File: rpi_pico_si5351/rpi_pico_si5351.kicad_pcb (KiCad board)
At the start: 4 copper layers, 100 x 50 mm, 39 parts, among them J1 CLK0, J2 CLK1, J3 CLK2, J4 SSM-120-F-DV, SW1 JS5208, SW2 PEC12R-3220F-S0024, U1 ER-TFT020-2, U2 RP2040-PICO30, U3 MS5351M, X1 MCSJK-7U-27.00-10-10-60-B-10

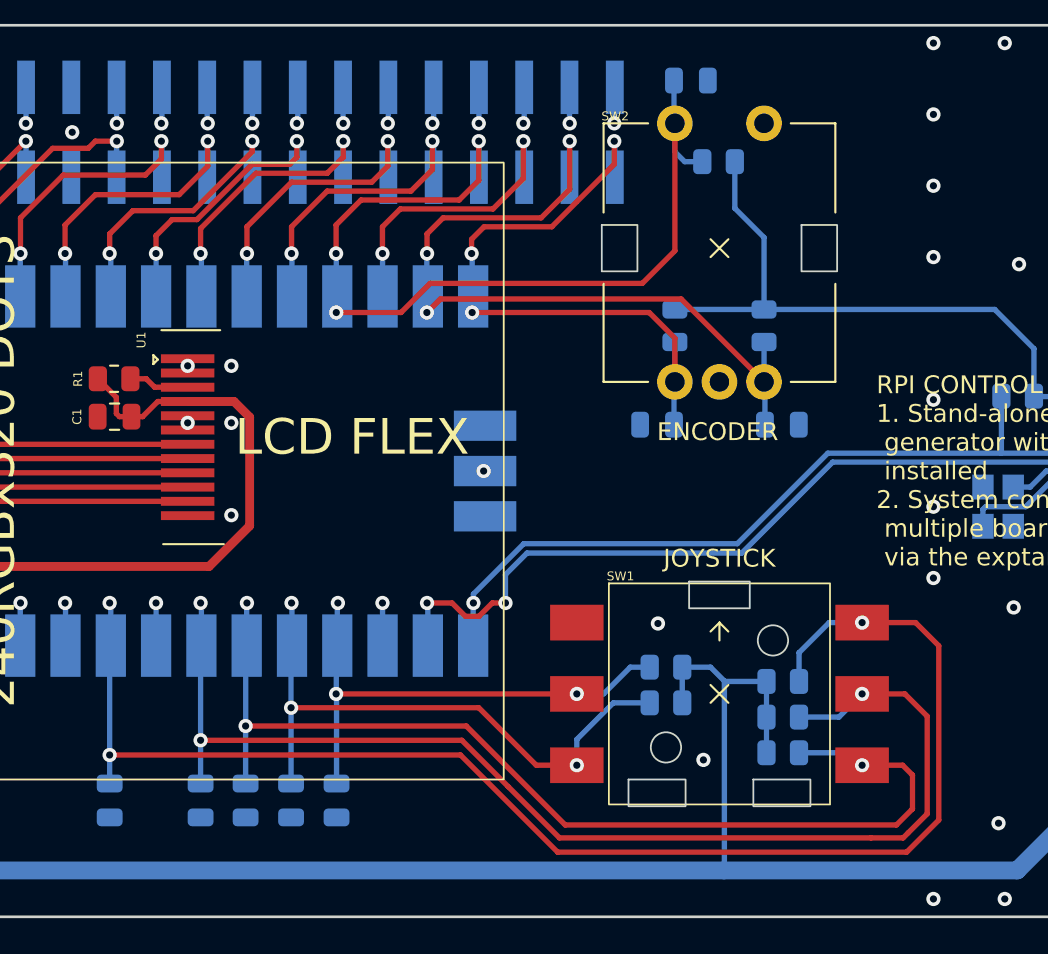
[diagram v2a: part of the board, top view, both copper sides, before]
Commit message: clean-up, add STACk connector
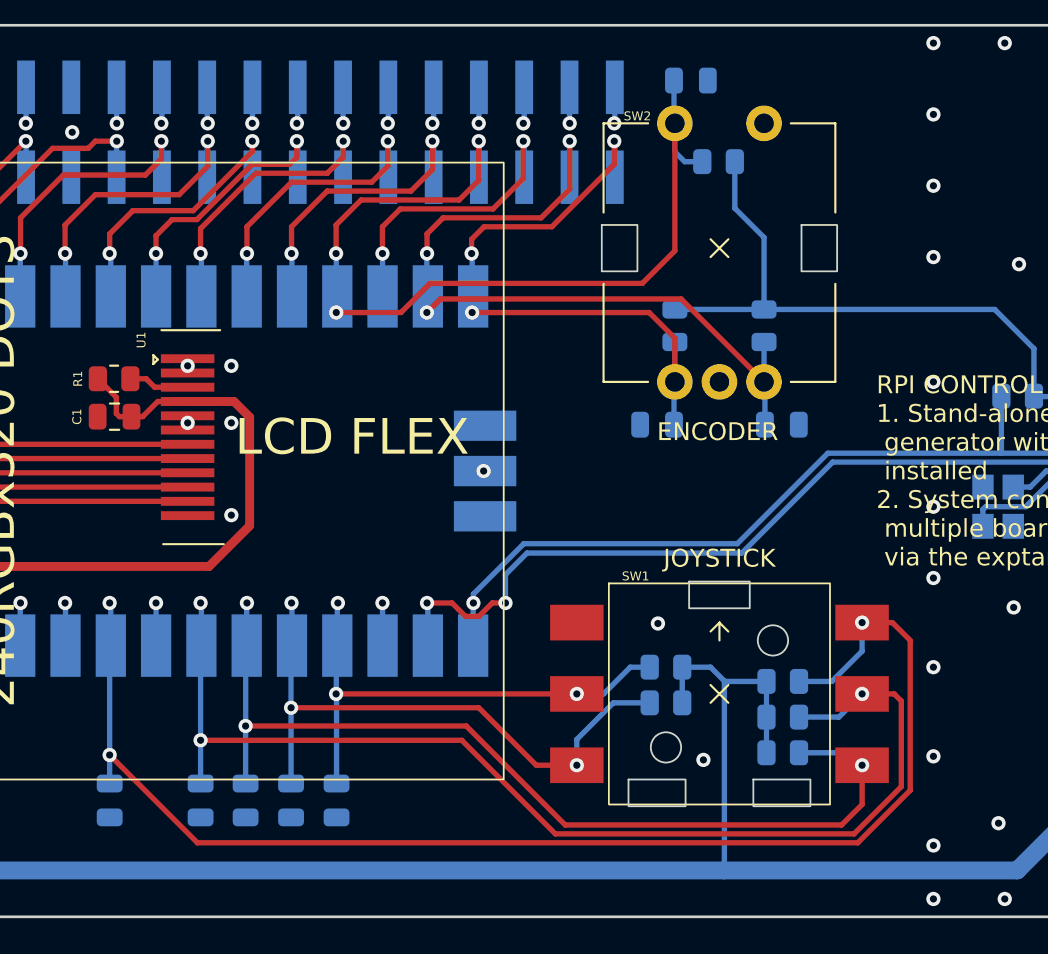
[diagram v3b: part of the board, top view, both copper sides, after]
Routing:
- net GPIO20: track 91.8 -> 86.3 mm
- net GPIO22: track 113.1 -> 108.7 mm
- net GPIO21: track 100.4 -> 96.9 mm
- net GND: vias 48 -> 51
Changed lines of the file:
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@@
     (property "Sheetname" "")
     (attr through_hole)
-    (fp_text reference "SW2" (at -5.85 -7.4 unlocked) (layer "F.SilkS")
+    (fp_text reference "SW2" (at -4.6 -7.4 unlocked) (layer "F.SilkS")
       (effects (font (size 0.5 0.5) (thickness 0.1)))
     )
@@
     (property "Sheetname" "")
     (attr smd)
-    (fp_text reference "SW1" (at -5.55 -6.6 unlocked) (layer "F.SilkS")
+    (fp_text reference "SW1" (at -4.7 -6.6 unlocked) (layer "F.SilkS")
       (effects (font (size 0.5 0.5) (thickness 0.1)))
     )
@@
   (via (at 124.95 52.5) (size 0.8) (drill 0.4) (layers "F.Cu" "B.Cu") (free) (net 1))
   (via (at 106 38) (size 0.8) (drill 0.4) (layers "F.Cu" "B.Cu") (free) (net 1))
+  (via (at 106 71) (size 0.8) (drill 0.4) (layers "F.Cu" "B.Cu") (free) (net 1))
   (via (at 37 37.8) (size 0.8) (drill 0.4) (layers "F.Cu" "B.Cu") (net 1))
   (via (at 106 34) (size 0.8) (drill 0.4) (layers "F.Cu" "B.Cu") (free) (net 1))
@@
   (via (at 116.15 64.35) (size 0.8) (drill 0.4) (layers "F.Cu" "B.Cu") (free) (net 1))
   (via (at 116.15 55.1) (size 0.8) (drill 0.4) (layers "F.Cu" "B.Cu") (free) (net 1))
+  (via (at 106 61) (size 0.8) (drill 0.4) (layers "F.Cu" "B.Cu") (free) (net 1))
   (via (at 118 26) (size 0.8) (drill 0.4) (layers "F.Cu" "B.Cu") (free) (net 1))
   (via (at 110 74) (size 0.8) (drill 0.4) (layers "F.Cu" "B.Cu") (free) (net 1))
@@
   (via (at 122.4 46.9) (size 0.8) (drill 0.4) (layers "F.Cu" "B.Cu") (free) (net 1))
   (via (at 80.775 50) (size 0.8) (drill 0.4) (layers "F.Cu" "B.Cu") (net 1))
+  (via (at 106 66) (size 0.8) (drill 0.4) (layers "F.Cu" "B.Cu") (free) (net 1))
   (via (at 106 74) (size 0.8) (drill 0.4) (layers "F.Cu" "B.Cu") (free) (net 1))
   (via (at 122 74) (size 0.8) (drill 0.4) (layers "F.Cu" "B.Cu") (free) (net 1))
   (via (at 110.5 57.65) (size 0.8) (drill 0.4) (layers "F.Cu" "B.Cu") (free) (net 1))
   (via (at 114 26) (size 0.8) (drill 0.4) (layers "F.Cu" "B.Cu") (free) (net 1))
-  (via (at 106 46) (size 0.8) (drill 0.4) (layers "F.Cu" "B.Cu") (free) (net 1))
+  (via (at 106 45) (size 0.8) (drill 0.4) (layers "F.Cu" "B.Cu") (free) (net 1))
   (via (at 124.95 59.5) (size 0.8) (drill 0.4) (layers "F.Cu" "B.Cu") (free) (net 1))
   (via (at 118 74) (size 0.8) (drill 0.4) (layers "F.Cu" "B.Cu") (free) (net 1))
@@
   (segment (start 72.565 58.89) (end 72.565 57.435) (width 0.3) (layer "B.Cu") (net 39))
   (segment (start 89 61) (end 90.0875 61) (width 0.3) (layer "B.Cu") (net 39))
-  (segment (start 105 58.5) (end 106.3 59.8) (width 0.3) (layer "F.Cu") (net 40))
-  (segment (start 106.3 69.575) (end 104.5 71.375) (width 0.3) (layer "F.Cu") (net 40))
-  (segment (start 106.3 59.8) (end 106.3 69.575) (width 0.3) (layer "F.Cu") (net 40))
-  (segment (start 79.475 65.925) (end 59.8 65.925) (width 0.3) (layer "F.Cu") (net 40))
-  (segment (start 84.925 71.375) (end 79.475 65.925) (width 0.3) (layer "F.Cu") (net 40))
-  (segment (start 104.5 71.375) (end 84.925 71.375) (width 0.3) (layer "F.Cu") (net 40))
-  (segment (start 102 58.5) (end 105 58.5) (width 0.3) (layer "F.Cu") (net 40))
+  (segment (start 104.7 67.907106) (end 101.757106 70.85) (width 0.3) (layer "F.Cu") (net 40))
+  (segment (start 103.7 58.5) (end 104.7 59.5) (width 0.3) (layer "F.Cu") (net 40))
+  (segment (start 64.725 70.85) (end 59.8 65.925) (width 0.3) (layer "F.Cu") (net 40))
+  (segment (start 104.7 59.5) (end 104.7 67.907106) (width 0.3) (layer "F.Cu") (net 40))
+  (segment (start 102 58.5) (end 103.7 58.5) (width 0.3) (layer "F.Cu") (net 40))
+  (segment (start 101.757106 70.85) (end 64.725 70.85) (width 0.3) (layer "F.Cu") (net 40))
   (via (at 59.8 65.925) (size 0.8) (drill 0.4) (layers "F.Cu" "B.Cu") (net 40))
   (via (at 59.8 57.4) (size 0.8) (drill 0.4) (layers "F.Cu" "B.Cu") (net 40))
@@
   (segment (start 59.8 58.9) (end 59.81 58.89) (width 0.3) (layer "B.Cu") (net 40))
   (segment (start 59.865 57.465) (end 59.8 57.4) (width 0.3) (layer "B.Cu") (net 40))
+  (segment (start 98.4625 61.8) (end 100.3 61.8) (width 0.3) (layer "B.Cu") (net 40))
+  (segment (start 100.3 61.8) (end 102 60.1) (width 0.3) (layer "B.Cu") (net 40))
   (segment (start 59.865 58.89) (end 59.865 57.465) (width 0.3) (layer "B.Cu") (net 40))
+  (segment (start 102 60.1) (end 102 58.5) (width 0.3) (layer "B.Cu") (net 40))
   (segment (start 67.81 30.490497) (end 67.8 30.500497) (width 0.3) (layer "B.Cu") (net 40))
   (segment (start 59.8 67.525) (end 59.8 65.925) (width 0.3) (layer "B.Cu") (net 40))
-  (segment (start 98.4625 61.8) (end 98.4625 60.1875) (width 0.3) (layer "B.Cu") (net 40))
   (segment (start 59.8 65.925) (end 59.8 58.9) (width 0.3) (layer "B.Cu") (net 40))
   (segment (start 67.81 28.48) (end 67.81 30.490497) (width 0.3) (layer "B.Cu") (net 40))
-  (segment (start 98.4625 60.1875) (end 100.15 58.5) (width 0.3) (layer "B.Cu") (net 40))
-  (segment (start 100.15 58.5) (end 102 58.5) (width 0.3) (layer "B.Cu") (net 40))
-  (segment (start 104.4 62.5) (end 105.65 63.75) (width 0.3) (layer "F.Cu") (net 41))
-  (segment (start 102 62.5) (end 104.4 62.5) (width 0.3) (layer "F.Cu") (net 41))
-  (segment (start 105.65 63.75) (end 105.65 69.225) (width 0.3) (layer "F.Cu") (net 41))
-  (segment (start 104.575 70.3) (end 104.3 70.575) (width 0.3) (layer "F.Cu") (net 41))
-  (segment (start 82.15 67.7) (end 79.55 65.1) (width 0.3) (layer "F.Cu") (net 41))
+  (segment (start 103.8 62.5) (end 104.2 62.9) (width 0.3) (layer "F.Cu") (net 41))
+  (segment (start 101.55 70.35) (end 84.8 70.35) (width 0.3) (layer "F.Cu") (net 41))
+  (segment (start 104.2 62.9) (end 104.2 67.7) (width 0.3) (layer "F.Cu") (net 41))
+  (segment (start 84.8 70.35) (end 79.55 65.1) (width 0.3) (layer "F.Cu") (net 41))
   (segment (start 79.55 65.1) (end 64.9 65.1) (width 0.3) (layer "F.Cu") (net 41))
-  (segment (start 105.65 69.225) (end 104.575 70.3) (width 0.3) (layer "F.Cu") (net 41))
-  (segment (start 102.5 70.575) (end 85.025 70.575) (width 0.3) (layer "F.Cu") (net 41))
-  (segment (start 104.3 70.575) (end 102.5 70.575) (width 0.3) (layer "F.Cu") (net 41))
-  (segment (start 85.025 70.575) (end 82.15 67.7) (width 0.3) (layer "F.Cu") (net 41))
+  (segment (start 104.2 67.7) (end 101.55 70.35) (width 0.3) (layer "F.Cu") (net 41))
+  (segment (start 102 62.5) (end 103.8 62.5) (width 0.3) (layer "F.Cu") (net 41))
   (via (at 64.9 65.1) (size 0.8) (drill 0.4) (layers "F.Cu" "B.Cu") (net 41))
   (via (at 102 62.5) (size 0.8) (drill 0.4) (layers "F.Cu" "B.Cu") (net 41))
@@
   (segment (start 64.9 65.1) (end 64.9 58.9) (width 0.3) (layer "B.Cu") (net 41))
   (segment (start 64.9 67.525) (end 64.9 65.1) (width 0.3) (layer "B.Cu") (net 41))
+  (segment (start 102 66.5) (end 102 68.7) (width 0.3) (layer "F.Cu") (net 42))
+  (segment (start 102 68.7) (end 100.85 69.85) (width 0.3) (layer "F.Cu") (net 42))
   (segment (start 79.8 64.3) (end 67.425 64.3) (width 0.3) (layer "F.Cu") (net 42))
-  (segment (start 104.825 68.95) (end 103.925 69.85) (width 0.3) (layer "F.Cu") (net 42))
-  (segment (start 104.275 66.5) (end 104.825 67.05) (width 0.3) (layer "F.Cu") (net 42))
-  (segment (start 104.825 67.05) (end 104.825 68.95) (width 0.3) (layer "F.Cu") (net 42))
-  (segment (start 103.925 69.85) (end 85.35 69.85) (width 0.3) (layer "F.Cu") (net 42))
-  (segment (start 102 66.5) (end 104.275 66.5) (width 0.3) (layer "F.Cu") (net 42))
+  (segment (start 100.85 69.85) (end 85.35 69.85) (width 0.3) (layer "F.Cu") (net 42))
   (segment (start 85.35 69.85) (end 79.8 64.3) (width 0.3) (layer "F.Cu") (net 42))
   (via (at 67.5 57.4) (size 0.8) (drill 0.4) (layers "F.Cu" "B.Cu") (net 42))
@@
     (polygon
       (pts
-        (xy 107 47)
-        (xy 105 47)
-        (xy 105 42.95)
-        (xy 107 42.95)
+        (xy 107 48)
+        (xy 105 48)
+        (xy 105 42)
+        (xy 107 42)
       )
     )
@@
     (connect_pads (clearance 0))
     (min_thickness 0.254) (filled_areas_thickness no)
-    (fill yes (thermal_gap 0.508) (thermal_bridge_width 0.508))
+    (fill yes (mode hatch) (thermal_gap 0.508) (thermal_bridge_width 0.508)
+      (hatch_thickness 1.016) (hatch_gap 1.524) (hatch_orientation 0)
+      (hatch_border_algorithm hatch_thickness) (hatch_min_hole_area 0.3))
     (polygon
       (pts
-        (xy 120.95 27)
+        (xy 123 27)
         (xy 107 27)
-        (xy 107 38.95)
-        (xy 105 38.95)
+        (xy 107 40)
+        (xy 105 40)
         (xy 105 25)
-        (xy 120.95 25)
+        (xy 123 25)
       )
     )
@@
         (xy 107 71.45)
         (xy 105 71.45)
-        (xy 105 51.5)
-        (xy 107 51.5)
+        (xy 105 51)
+        (xy 107 51)
       )
     )

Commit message: production data
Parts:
- moved C1 1.08 mm to (59.0, 47.0)
- moved R1 1.05 mm to (59.0, 44.8), turned to 0 degrees
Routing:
- net Net-(R1-Pad1): track 3.41 -> 8.27 mm
- net GPIO22: track 108.7 -> 109.4 mm
- net GPIO19: track 66.9 -> 67.5 mm
- net GPIO21: track 96.9 -> 97.6 mm
- net GND: vias 51 -> 44
